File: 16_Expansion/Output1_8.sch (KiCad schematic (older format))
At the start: 20 parts, among them J1 String1, J2 String2, J3 String3, J4 String4, J5 String5, J6 String6, J7 String7, J8 String8, U1 SN74HCT245N

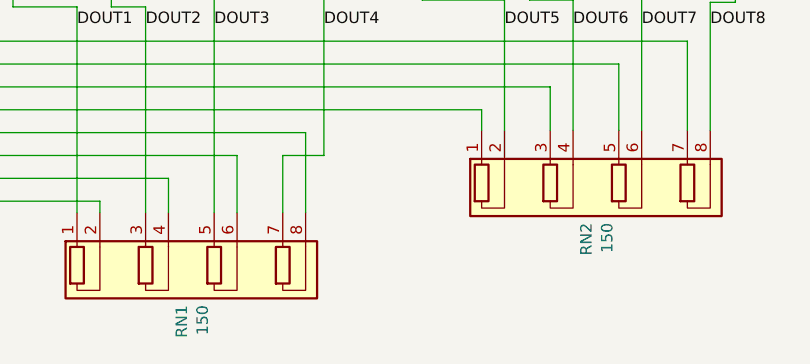
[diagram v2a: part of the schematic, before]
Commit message: Updated Pixel Pixel resistor packs to 33ohms
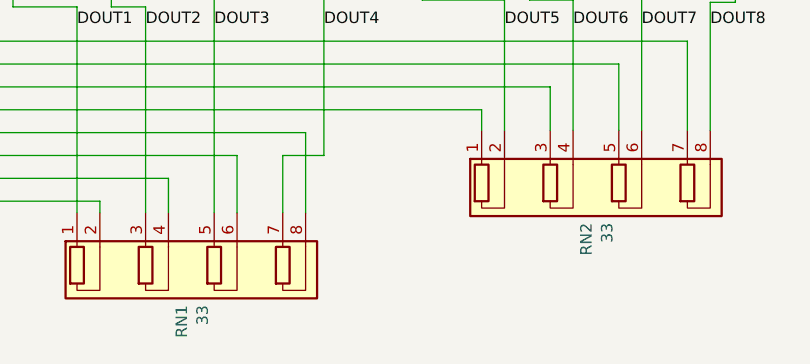
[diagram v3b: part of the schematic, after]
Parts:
- RN1, RN2: value 150 -> 33; Digi-Key_PN 4608X-2-151LF-ND -> 4608X-2-330LF-ND; MPN 4608X-102-151LF -> 4608X-102-330LF
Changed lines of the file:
@@
 AR Path="/5D469293/5D4CFC06" Ref="RN2"  Part="1"
 F 0 "RN2" V 8158 5285 50  0000 L CNN
-F 1 "150" V 8249 5285 50  0000 L CNN
+F 1 "33" V 8249 5285 50  0000 L CNN
 F 2 "Resistor_THT:R_Array_SIP8" V 8875 5080 50  0001 C CNN
 F 3 "http://www.vishay.com/docs/31509/csc.pdf" H 8200 5080 50  0001 C CNN
-F 4 "4608X-2-151LF-ND" H -1460 50  50  0001 C CNN "Digi-Key_PN"
-F 5 "4608X-102-151LF" H -1460 50  50  0001 C CNN "MPN"
+F 4 "4608X-2-330LF-ND" H -1460 50  50  0001 C CNN "Digi-Key_PN"
+F 5 "4608X-102-330LF" H -1460 50  50  0001 C CNN "MPN"
 	1    8200 5080
 	1    0    0    1
@@
 AR Path="/5D469293/5D4CFC39" Ref="RN1"  Part="1"
 F 0 "RN1" V 6388 5645 50  0000 L CNN
-F 1 "150" V 6479 5645 50  0000 L CNN
+F 1 "33" V 6479 5645 50  0000 L CNN
 F 2 "Resistor_THT:R_Array_SIP8" V 7105 5440 50  0001 C CNN
 F 3 "http://www.vishay.com/docs/31509/csc.pdf" H 6430 5440 50  0001 C CNN
-F 4 "4608X-2-151LF-ND" H -1260 450 50  0001 C CNN "Digi-Key_PN"
-F 5 "4608X-102-151LF" H -1260 450 50  0001 C CNN "MPN"
+F 4 "4608X-2-330LF-ND" H -1260 450 50  0001 C CNN "Digi-Key_PN"
+F 5 "4608X-102-330LF" H -1260 450 50  0001 C CNN "MPN"
 	1    6430 5440
 	1    0    0    1
